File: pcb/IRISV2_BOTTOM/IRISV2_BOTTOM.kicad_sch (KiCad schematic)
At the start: 43 parts, among them J1 Screw_Terminal_01x02, J3 Conn_01x20_MountingPin, Q17 BC846, U1 TPS613222ADBV, U2 INA237, U3 MP4323GDE-Z

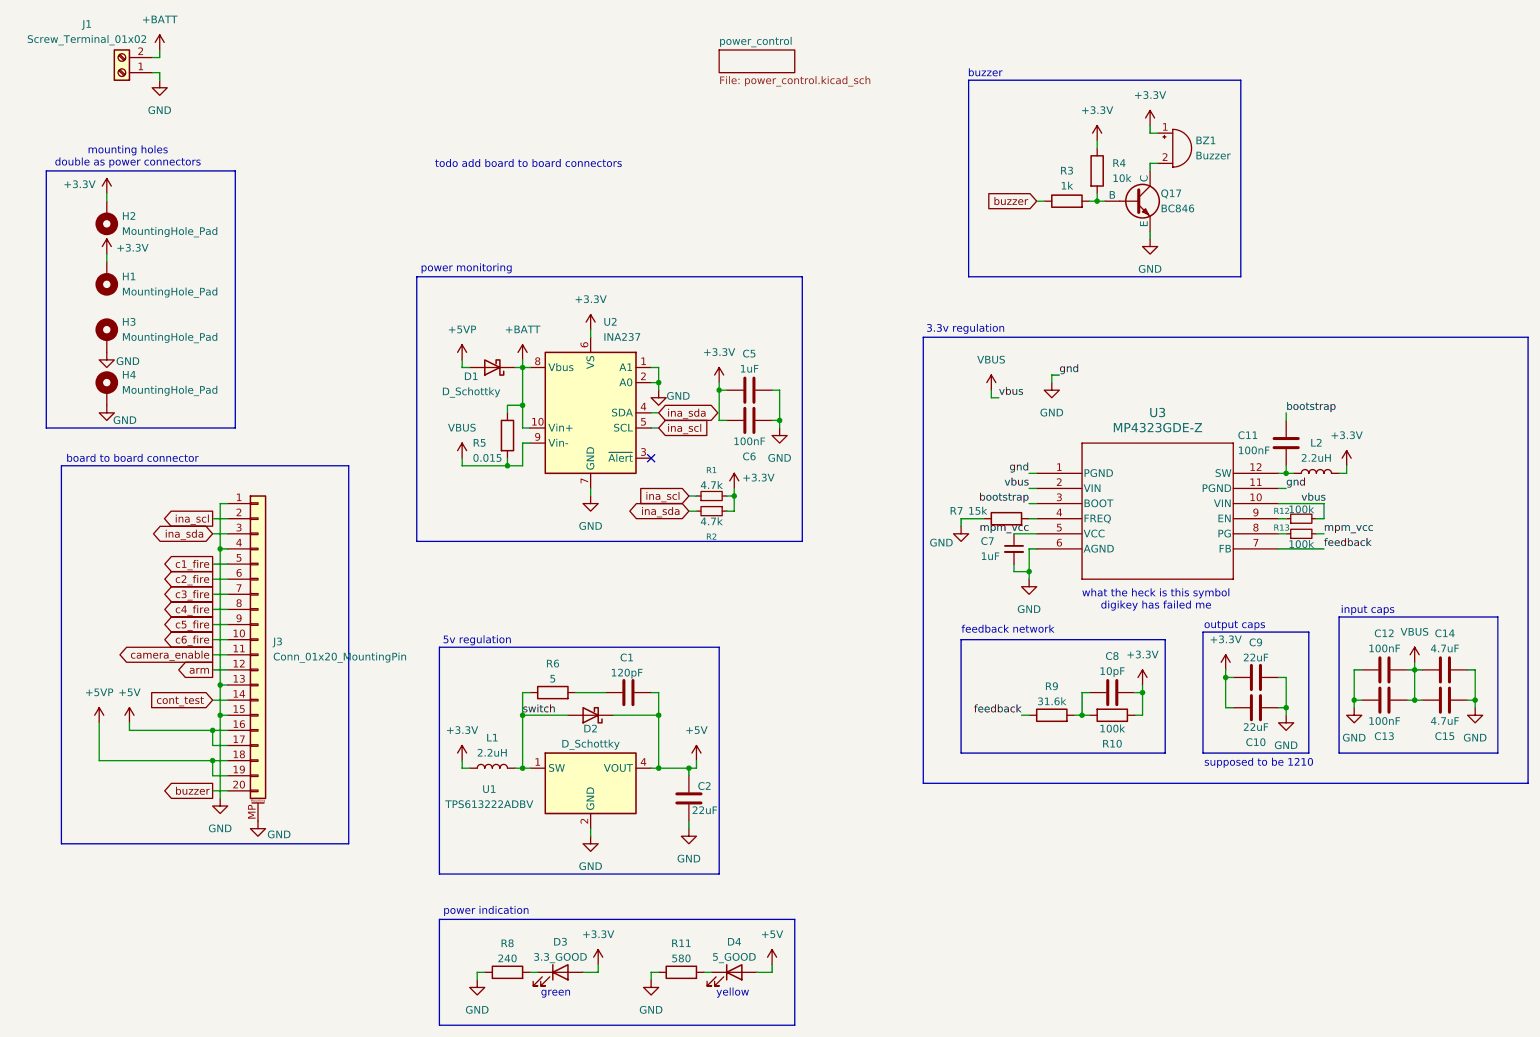
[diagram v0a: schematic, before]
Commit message: all main routing done, need to break out remaining gpio onto banks of mpu and ppu
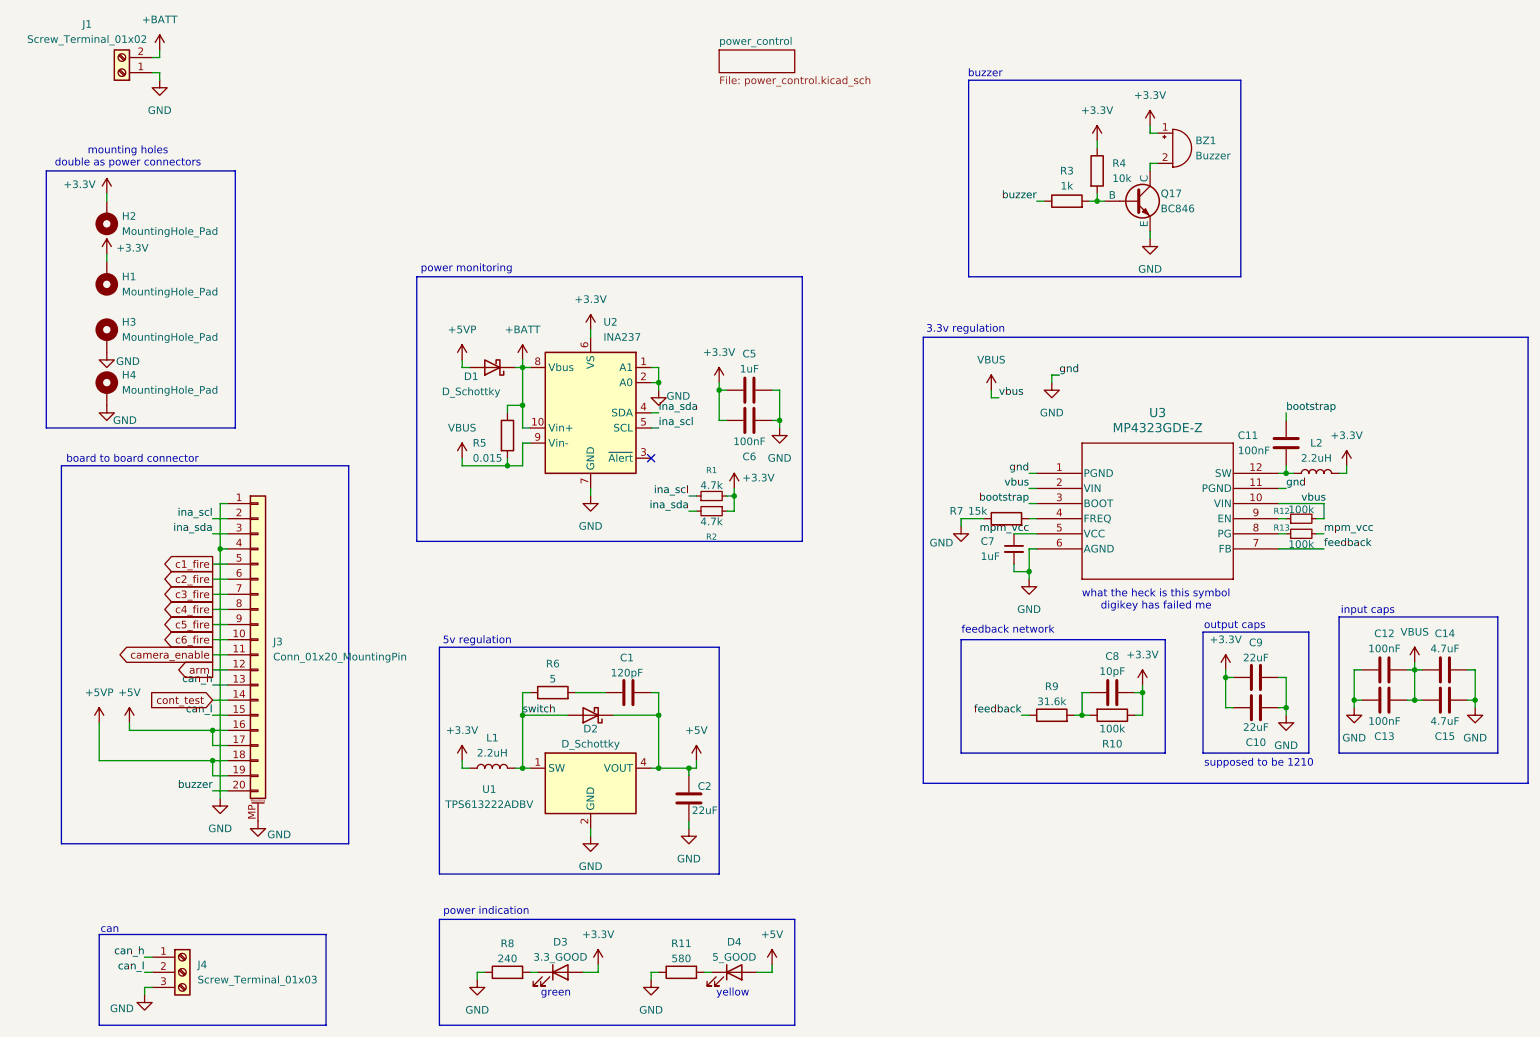
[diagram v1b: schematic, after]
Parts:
- added J4: Screw_Terminal_01x03, OSTTE030104:OSTTE030104, symbol Connector:Screw_Terminal_01x03
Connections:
- net GND: now also J4.3 (Pin_3); no longer J3.13 (Pin_13), J3.15 (Pin_15)
- new net can_h: J3.13 (Pin_13), J4.1 (Pin_1)
- new net can_l: J3.15 (Pin_15), J4.2 (Pin_2)
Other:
- note added: "can"
- note removed: "todo add board to board connectors"

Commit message: fixed some issues, lr2021 matching is now 0201 - todo change trace width to match pad width like ref design, see todo for rest
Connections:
- net GND: now also R9.1
- net feedback: now also C8.1, R10.2, R9.2; no longer R9.1
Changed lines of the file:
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@@
 	(wire
 		(pts
+			(xy 184.15 134.62) (xy 184.15 135.89)
+		)
+		(stroke
+			(width 0)
+			(type default)
+		)
+	)
+	(wire
+		(pts
 			(xy 101.6 177.8) (xy 102.87 177.8)
 		)
@@
 		)
 	)
+	(label "feedback"
+		(at 194.31 130.81 180)
+		(effects
+			(font
+				(size 1.27 1.27)
+			)
+			(justify right bottom)
+		)
+	)
 	(label "buzzer"
 		(at 48.26 147.32 180)
@@
 		)
 	)
-	(label "feedback"
-		(at 184.15 134.62 180)
-		(effects
-			(font
-				(size 1.27 1.27)
-			)
-			(justify right bottom)
-		)
-	)
 	(label "buzzer"
 		(at 186.69 48.26 180)
@@
 		(dnp no)
 		(property "Reference" "R9"
-			(at 189.23 129.794 90)
+			(at 189.23 136.652 90)
 			(effects
 				(font
@@
 		)
 		(property "Value" "31.6k"
-			(at 189.23 132.334 90)
+			(at 189.23 139.192 90)
 			(effects
 				(font
@@
 					(unit 1)
 				)
+			)
+		)
+	)
+	(symbol
+		(lib_id "power:GND")
+		(at 184.15 135.89 0)
+		(unit 1)
+		(exclude_from_sim no)
+		(in_bom yes)
+		(on_board yes)
+		(dnp no)
+		(property "Reference" "#PWR042"
+			(at 184.15 142.24 0)
+			(effects
+				(font
+					(size 1.27 1.27)
+				)
+				(hide yes)
+			)
+		)
+		(property "Value" "GND"
+			(at 180.594 137.922 0)
+			(effects
+				(font
+					(size 1.27 1.27)
+				)
+			)
+		)
+		(property "Footprint" ""
+			(at 184.15 135.89 0)
+			(effects
+				(font
+					(size 1.27 1.27)
+				)
+				(hide yes)
+			)
+		)
+		(property "Datasheet" ""
+			(at 184.15 135.89 0)
+			(effects
+				(font
+					(size 1.27 1.27)
+				)
+				(hide yes)
+			)
+		)
+		(property "Description" "Power symbol creates a global label with name \"GND\" , ground"
+			(at 184.15 135.89 0)
+			(effects
+				(font
+					(size 1.27 1.27)
+				)
+				(hide yes)
+			)
+		)
+		(pin "1"
+		)
+		(instances
+			(project "IRISV2_BOTTOM"
+				(path "/27a5960f-7325-4718-9a51-5d24e2b80910"
+					(reference "#PWR042")
+					(unit 1)
+				)

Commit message: removed usb, added connectors and stuff, 3d models mostly added, still need to route out gpio and servos (though connectors added)
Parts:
- L2: footprint MGAH0603:MGAH0603 -> SPR5020TA-2R2M:SRP5020TA2R2M
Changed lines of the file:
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@@
 			)
 		)
-		(property "Footprint" "MGAH0603:MGAH0603"
+		(property "Footprint" "SPR5020TA-2R2M:SRP5020TA2R2M"
 			(at 233.68 93.98 0)
 			(effects

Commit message: pcb hopefully mostly finalized
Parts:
- added J2: Conn_01x02, Connector_PinHeader_2.54mm:PinHeader_1x02_P2.54mm_Vertical, symbol Connector_Generic:Conn_01x02
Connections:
- net GND: no longer J3.1 (Pin_1), J3.4 (Pin_4)
- new net cam_uart_rx: J2.2 (Pin_2), J3.4 (Pin_4)
- new net cam_uart_tx: J2.1 (Pin_1), J3.1 (Pin_1)
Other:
- note added: "camera uart"
